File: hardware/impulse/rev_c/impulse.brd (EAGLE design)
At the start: 32.5 x 13 mm, 52 parts, among them J2 EPIC-PROG-POGO-NO-LEGS, J3 IMPULSE_GECKO_HEADER, Q1 MOSFET-NCHANNELXFDN-3, U1 DS2411, U2 FM25LBTDFN-8, U3 MSP430F1611IRTD, U4 CC2420RGZ, X1 TXC-7V, X2 ABRACON-ABS05

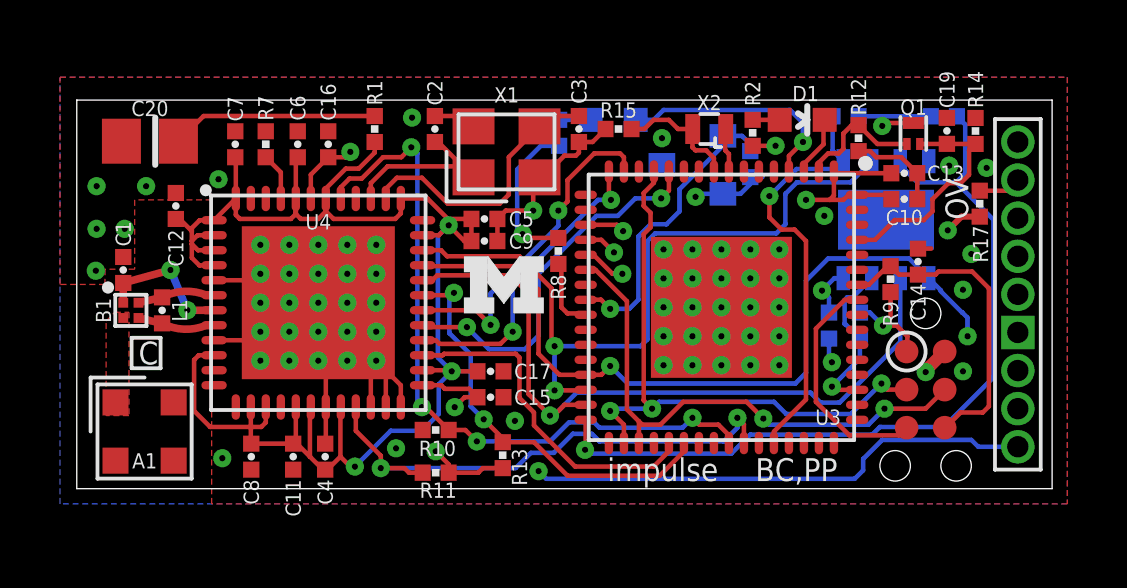
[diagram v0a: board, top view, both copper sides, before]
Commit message: updated rev c.
new solder jumpers

straightened some traces

added some vias for planes
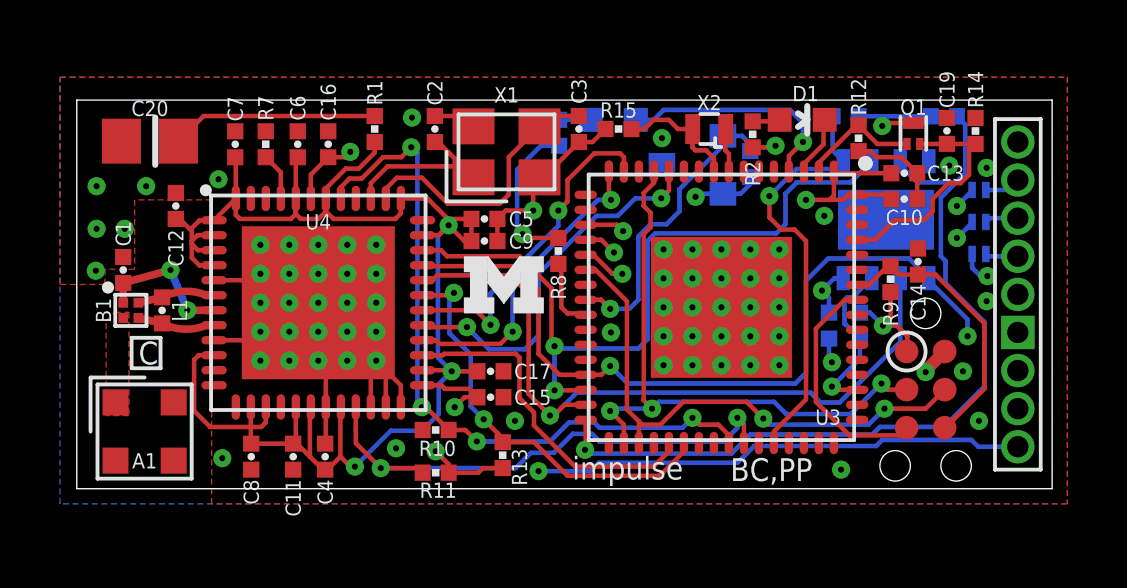
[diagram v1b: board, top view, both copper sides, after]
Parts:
- removed R17: 0, passives:0402_RES
- added SJ1, SJ2, SJ3: SJ, passives:SJ-0202
- moved R2 0.05 mm to (22.5, 11.8), turned to 90 degrees
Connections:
- new net N$10: J3.2, SJ1.1
- new net N$11: J3.3, SJ2.1
- net N$6: now also R2.2; no longer R2.1
- net OV: now also SJ3.2; no longer R17.2
- net OV-HEADER: now also SJ3.1; no longer R17.1
- net SHD: now also SJ2.2; no longer J3.3
- net TRIG: now also SJ1.2; no longer J3.2
- net VCC: now also R2.1; no longer R2.2
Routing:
- net SHD: track 15.8 -> 14.3 mm, vias 1 -> 2
- net !RESET: track 10.8 -> 9.36 mm
- net N$11: track 0.00 -> 1.12 mm
- net N$10: track 0.00 -> 1.10 mm
- net GND: track 31.2 -> 30.6 mm, vias 70 -> 72
- net TRIG: track 16.4 -> 16.3 mm, vias 1 -> 2
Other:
- board text added: "2013/10/21"
- board text added: "SHTD"
- board text added: "TRIG"
- board text removed: "2013/10/09"
- board text removed: "OVERVOLT"
- board text removed: "SHUTDOWN"
- board text removed: "TRIGGER"
